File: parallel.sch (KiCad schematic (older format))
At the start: 74 parts, among them CN300 KEYBOARD, CN301 DB25F, CN302 DB23F, CN303 Conn_02x17_Odd_Even, J300 Conn_01x03_Male, J301 DF1:, Q301 2N3904, U102 GARY5719, U108 74LS74A, U203 74LS38, U300 CIA8520, U302 74LS32, U303 74F08, U607 74LS08, U900 74F00

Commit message: Update footprints
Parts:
- C203, C259, C260, C261, C300, C302, C303, C322, C323, C607, C909, C916: footprint (none) -> Capacitor_THT:C_Rect_L11.0mm_W2.8mm_P10.00mm_MKT
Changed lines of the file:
@@
 F 0 "C261" H 9115 1846 50  0000 L CNN
 F 1 "100pF" H 9115 1755 50  0000 L CNN
-F 2 "" H 9038 1650 50  0001 C CNN
+F 2 "Capacitor_THT:C_Rect_L11.0mm_W2.8mm_P10.00mm_MKT" H 9038 1650 50  0001 C CNN
 F 3 "~" H 9000 1800 50  0001 C CNN
 	1    9000 1800
@@
 F 0 "C260" H 9565 1846 50  0000 L CNN
 F 1 "100pF" H 9565 1755 50  0000 L CNN
-F 2 "" H 9488 1650 50  0001 C CNN
+F 2 "Capacitor_THT:C_Rect_L11.0mm_W2.8mm_P10.00mm_MKT" H 9488 1650 50  0001 C CNN
 F 3 "~" H 9450 1800 50  0001 C CNN
 	1    9450 1800
@@
 F 0 "C259" H 10015 1846 50  0000 L CNN
 F 1 "100pF" H 10015 1755 50  0000 L CNN
-F 2 "" H 9938 1650 50  0001 C CNN
+F 2 "Capacitor_THT:C_Rect_L11.0mm_W2.8mm_P10.00mm_MKT" H 9938 1650 50  0001 C CNN
 F 3 "~" H 9900 1800 50  0001 C CNN
 	1    9900 1800
@@
 F 0 "C909" H 3415 6046 50  0000 L CNN
 F 1 "0.1uF" H 3415 5955 50  0000 L CNN
-F 2 "" H 3338 5850 50  0001 C CNN
+F 2 "Capacitor_THT:C_Rect_L11.0mm_W2.8mm_P10.00mm_MKT" H 3338 5850 50  0001 C CNN
 F 3 "~" H 3300 6000 50  0001 C CNN
 	1    3300 6000
@@
 F 0 "C916" H 8215 7446 50  0000 L CNN
 F 1 "0.1uF" H 8215 7355 50  0000 L CNN
-F 2 "" H 8138 7250 50  0001 C CNN
+F 2 "Capacitor_THT:C_Rect_L11.0mm_W2.8mm_P10.00mm_MKT" H 8138 7250 50  0001 C CNN
 F 3 "~" H 8100 7400 50  0001 C CNN
 	1    8100 7400
@@
 F 0 "C322" H 15265 2046 50  0000 L CNN
 F 1 "0.01uF" H 15265 1955 50  0000 L CNN
-F 2 "" H 15188 1850 50  0001 C CNN
+F 2 "Capacitor_THT:C_Rect_L11.0mm_W2.8mm_P10.00mm_MKT" H 15188 1850 50  0001 C CNN
 F 3 "~" H 15150 2000 50  0001 C CNN
 	1    15150 2000
@@
 F 0 "C323" H 15765 2046 50  0000 L CNN
 F 1 "0.01uF" H 15765 1955 50  0000 L CNN
-F 2 "" H 15688 1850 50  0001 C CNN
+F 2 "Capacitor_THT:C_Rect_L11.0mm_W2.8mm_P10.00mm_MKT" H 15688 1850 50  0001 C CNN
 F 3 "~" H 15650 2000 50  0001 C CNN
 	1    15650 2000
@@
 F 0 "C300" H 2865 2846 50  0000 L CNN
 F 1 "0.1uF" H 2865 2755 50  0000 L CNN
-F 2 "" H 2788 2650 50  0001 C CNN
+F 2 "Capacitor_THT:C_Rect_L11.0mm_W2.8mm_P10.00mm_MKT" H 2788 2650 50  0001 C CNN
 F 3 "~" H 2750 2800 50  0001 C CNN
 	1    2750 2800
@@
 F 0 "C203" H 2815 10046 50  0000 L CNN
 F 1 "0.1uF" H 2815 9955 50  0000 L CNN
-F 2 "" H 2738 9850 50  0001 C CNN
+F 2 "Capacitor_THT:C_Rect_L11.0mm_W2.8mm_P10.00mm_MKT" H 2738 9850 50  0001 C CNN
 F 3 "~" H 2700 10000 50  0001 C CNN
 	1    2700 10000
@@
 F 0 "C302" H 4515 10046 50  0000 L CNN
 F 1 "0.1uF" H 4515 9955 50  0000 L CNN
-F 2 "" H 4438 9850 50  0001 C CNN
+F 2 "Capacitor_THT:C_Rect_L11.0mm_W2.8mm_P10.00mm_MKT" H 4438 9850 50  0001 C CNN
 F 3 "~" H 4400 10000 50  0001 C CNN
 	1    4400 10000
@@
 F 0 "C303" H 6215 10046 50  0000 L CNN
 F 1 "0.1uF" H 6215 9955 50  0000 L CNN
-F 2 "" H 6138 9850 50  0001 C CNN
+F 2 "Capacitor_THT:C_Rect_L11.0mm_W2.8mm_P10.00mm_MKT" H 6138 9850 50  0001 C CNN
 F 3 "~" H 6100 10000 50  0001 C CNN
 	1    6100 10000
@@
 F 0 "C607" H 7715 9996 50  0000 L CNN
 F 1 "0.1uF" H 7715 9905 50  0000 L CNN
-F 2 "" H 7638 9800 50  0001 C CNN
+F 2 "Capacitor_THT:C_Rect_L11.0mm_W2.8mm_P10.00mm_MKT" H 7638 9800 50  0001 C CNN
 F 3 "~" H 7600 9950 50  0001 C CNN
 	1    7600 9950
@@
 Wire Wire Line
 	15200 3600 15200 3650
+Text Notes 9650 5400 1    197  ~ 0
+PARALLEL
+Text Notes 13600 1950 2    197  ~ 0
+EXT FLOPPY
 Wire Bus Line
 	1200 4450 3050 4450
@@
 Wire Bus Line
 	4950 5000 4950 5900
-Text Notes 9650 5400 1    197  ~ 0
-PARALLEL
-Text Notes 13600 1950 2    197  ~ 0
-EXT FLOPPY
 $EndSCHEMATC

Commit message: Components associations finished; regenered netlist and pdf
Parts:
- CN300: footprint (none) -> d_amiga:DIN_5_KBD
- CN302: footprint (none) -> d_amiga:DSUB-23_Male_Horizontal_P2.77x2.84mm_EdgePinOffset7.70mm_Housed_MountingHolesOffset9.12mm
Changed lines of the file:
@@
 F 0 "CN302" V 12785 2450 50  0000 C CNN
 F 1 "DB23F" V 12876 2450 50  0000 C CNN
-F 2 "" H 13100 2350 50  0001 C CNN
+F 2 "d_amiga:DSUB-23_Male_Horizontal_P2.77x2.84mm_EdgePinOffset7.70mm_Housed_MountingHolesOffset9.12mm" H 13100 2350 50  0001 C CNN
 F 3 " ~" H 13100 2350 50  0001 C CNN
 F 4 "Female" V 13150 2450 50  0001 C CNN "Gender"
@@
 F 0 "CN300" H 10100 833 50  0000 C CNN
 F 1 "KEYBOARD" H 10100 924 50  0000 C CNN
-F 2 "" H 10100 1200 50  0001 C CNN
+F 2 "d_amiga:DIN_5_KBD" H 10100 1200 50  0001 C CNN
 F 3 "http://www.mouser.com/ds/2/18/40_c091_abd_e-75918.pdf" H 10100 1200 50  0001 C CNN
 F 4 "Female" H 10100 1200 50  0001 C CNN "Gender"

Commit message: More placement
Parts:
- CN303: footprint Connector_PinSocket_2.54mm:PinSocket_2x17_P2.54mm_Vertical -> Connector_PinHeader_2.54mm:PinHeader_2x17_P2.54mm_Vertical
- J300: footprint Connector_PinSocket_2.54mm:PinSocket_1x03_P2.54mm_Vertical -> Connector_PinHeader_2.54mm:PinHeader_1x03_P2.54mm_Vertical
- J301: footprint Connector_PinSocket_2.54mm:PinSocket_2x01_P2.54mm_Vertical -> Connector_PinHeader_2.54mm:PinHeader_2x01_P2.54mm_Vertical
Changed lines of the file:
@@
 F 0 "CN303" H 15700 6325 50  0000 C CNN
 F 1 "Conn_02x17_Odd_Even" H 15700 6326 50  0001 C CNN
-F 2 "Connector_PinSocket_2.54mm:PinSocket_2x17_P2.54mm_Vertical" H 15650 5400 50  0001 C CNN
+F 2 "Connector_PinHeader_2.54mm:PinHeader_2x17_P2.54mm_Vertical" H 15650 5400 50  0001 C CNN
 F 3 "~" H 15650 5400 50  0001 C CNN
 F 4 "Male" H 15650 5400 50  0001 C CNN "Gender"
@@
 F 0 "J300" V 2058 5812 50  0000 R CNN
 F 1 "Conn_01x03_Male" V 2013 5812 50  0001 R CNN
-F 2 "Connector_PinSocket_2.54mm:PinSocket_1x03_P2.54mm_Vertical" H 1950 6000 50  0001 C CNN
+F 2 "Connector_PinHeader_2.54mm:PinHeader_1x03_P2.54mm_Vertical" H 1950 6000 50  0001 C CNN
 F 3 "~" H 1950 6000 50  0001 C CNN
 	1    1950 6000
@@
 F 0 "J301" H 15572 6882 50  0000 R CNN
 F 1 "DF1:" H 15572 6973 50  0000 R CNN
-F 2 "Connector_PinSocket_2.54mm:PinSocket_2x01_P2.54mm_Vertical" H 15600 7000 50  0001 C CNN
+F 2 "Connector_PinHeader_2.54mm:PinHeader_2x01_P2.54mm_Vertical" H 15600 7000 50  0001 C CNN
 F 3 "~" H 15600 7000 50  0001 C CNN
 	1    15600 7000

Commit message: first placement pass is done
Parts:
- C912: footprint Capacitor_THT:CP_Radial_D10.0mm_P5.00mm -> Capacitor_THT:CP_Radial_D8.0mm_P5.00mm
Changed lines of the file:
@@
 F 0 "C912" H 10468 1846 50  0000 L CNN
 F 1 "470uF 25v" H 10468 1755 50  0000 L CNN
-F 2 "Capacitor_THT:CP_Radial_D10.0mm_P5.00mm" H 10388 1650 50  0001 C CNN
+F 2 "Capacitor_THT:CP_Radial_D8.0mm_P5.00mm" H 10388 1650 50  0001 C CNN
 F 3 "~" H 10350 1800 50  0001 C CNN
 	1    10350 1800

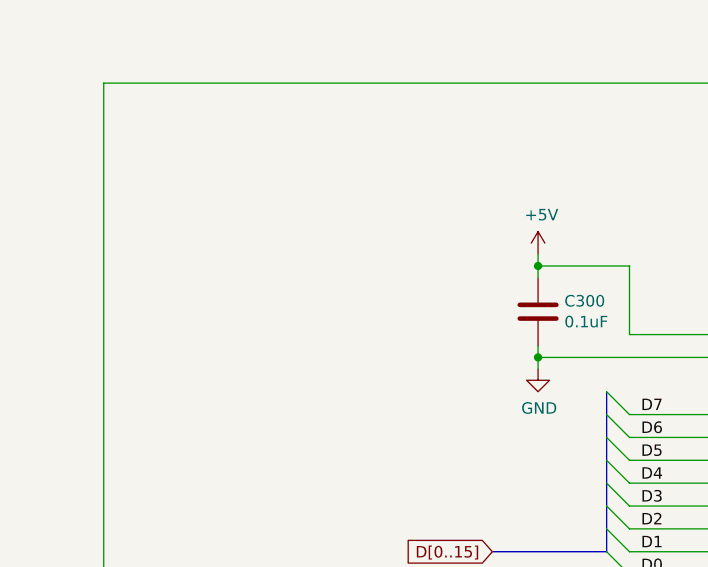
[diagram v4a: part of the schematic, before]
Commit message: mod: breakout INT2/OVR to pin header
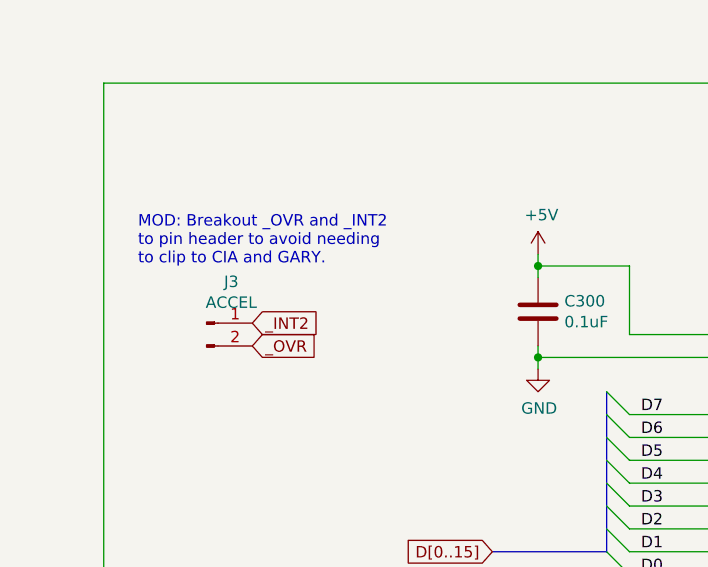
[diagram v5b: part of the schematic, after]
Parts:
- added J3: ACCEL, Connector_PinHeader_2.54mm:PinHeader_1x02_P2.54mm_Vertical, symbol Connector:Conn_01x02_Male
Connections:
- net _INT2: now also J3.1 (Pin_1)
- new net _OVR: J3.2 (Pin_2)
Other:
- note added: "MOD: Breakout _OVR and _INT2 \nto pin header to avoid needing \nto clip to CIA and GARY."
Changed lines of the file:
@@
 Text Notes 13600 1950 2    197  ~ 0
 EXT FLOPPY
+$Comp
+L Connector:Conn_01x02_Male J3
+U 1 1 5E049EEE
+P 1300 2850
+F 0 "J3" H 1408 3031 50  0000 C CNN
+F 1 "ACCEL" H 1408 2940 50  0000 C CNN
+F 2 "Connector_PinHeader_2.54mm:PinHeader_1x02_P2.54mm_Vertical" H 1300 2850 50  0001 C CNN
+F 3 "~" H 1300 2850 50  0001 C CNN
+	1    1300 2850
+	1    0    0    -1
+$EndComp
+Text GLabel 1500 2850 2    50   Input ~ 0
+_INT2
+Text GLabel 1500 2950 2    50   Input ~ 0
+_OVR
+Text Notes 1000 2600 0    50   ~ 0
+MOD: Breakout _OVR and _INT2 \nto pin header to avoid needing \nto clip to CIA and GARY.
 Wire Bus Line
 	1200 4450 3050 4450

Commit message: Make caps footprint smaller
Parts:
- C203, C259, C260, C261, C300, C302, C303, C322, C323, C607, C909, C916: footprint Capacitor_THT:C_Rect_L11.0mm_W2.8mm_P10.00mm_MKT -> Capacitor_THT:C_Rect_L11.5mm_W2.0mm_P10.00mm_MKT
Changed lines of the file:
@@
 F 0 "C261" H 9115 1846 50  0000 L CNN
 F 1 "100pF" H 9115 1755 50  0000 L CNN
-F 2 "Capacitor_THT:C_Rect_L11.0mm_W2.8mm_P10.00mm_MKT" H 9038 1650 50  0001 C CNN
+F 2 "Capacitor_THT:C_Rect_L11.5mm_W2.0mm_P10.00mm_MKT" H 9038 1650 50  0001 C CNN
 F 3 "~" H 9000 1800 50  0001 C CNN
 	1    9000 1800
@@
 F 0 "C260" H 9565 1846 50  0000 L CNN
 F 1 "100pF" H 9565 1755 50  0000 L CNN
-F 2 "Capacitor_THT:C_Rect_L11.0mm_W2.8mm_P10.00mm_MKT" H 9488 1650 50  0001 C CNN
+F 2 "Capacitor_THT:C_Rect_L11.5mm_W2.0mm_P10.00mm_MKT" H 9488 1650 50  0001 C CNN
 F 3 "~" H 9450 1800 50  0001 C CNN
 	1    9450 1800
@@
 F 0 "C259" H 10015 1846 50  0000 L CNN
 F 1 "100pF" H 10015 1755 50  0000 L CNN
-F 2 "Capacitor_THT:C_Rect_L11.0mm_W2.8mm_P10.00mm_MKT" H 9938 1650 50  0001 C CNN
+F 2 "Capacitor_THT:C_Rect_L11.5mm_W2.0mm_P10.00mm_MKT" H 9938 1650 50  0001 C CNN
 F 3 "~" H 9900 1800 50  0001 C CNN
 	1    9900 1800
@@
 F 0 "C909" H 3415 6046 50  0000 L CNN
 F 1 "0.1uF" H 3415 5955 50  0000 L CNN
-F 2 "Capacitor_THT:C_Rect_L11.0mm_W2.8mm_P10.00mm_MKT" H 3338 5850 50  0001 C CNN
+F 2 "Capacitor_THT:C_Rect_L11.5mm_W2.0mm_P10.00mm_MKT" H 3338 5850 50  0001 C CNN
 F 3 "~" H 3300 6000 50  0001 C CNN
 	1    3300 6000
@@
 F 0 "C916" H 8215 7446 50  0000 L CNN
 F 1 "0.1uF" H 8215 7355 50  0000 L CNN
-F 2 "Capacitor_THT:C_Rect_L11.0mm_W2.8mm_P10.00mm_MKT" H 8138 7250 50  0001 C CNN
+F 2 "Capacitor_THT:C_Rect_L11.5mm_W2.0mm_P10.00mm_MKT" H 8138 7250 50  0001 C CNN
 F 3 "~" H 8100 7400 50  0001 C CNN
 	1    8100 7400
@@
 F 0 "C322" H 15265 2046 50  0000 L CNN
 F 1 "0.01uF" H 15265 1955 50  0000 L CNN
-F 2 "Capacitor_THT:C_Rect_L11.0mm_W2.8mm_P10.00mm_MKT" H 15188 1850 50  0001 C CNN
+F 2 "Capacitor_THT:C_Rect_L11.5mm_W2.0mm_P10.00mm_MKT" H 15188 1850 50  0001 C CNN
 F 3 "~" H 15150 2000 50  0001 C CNN
 	1    15150 2000
@@
 F 0 "C323" H 15765 2046 50  0000 L CNN
 F 1 "0.01uF" H 15765 1955 50  0000 L CNN
-F 2 "Capacitor_THT:C_Rect_L11.0mm_W2.8mm_P10.00mm_MKT" H 15688 1850 50  0001 C CNN
+F 2 "Capacitor_THT:C_Rect_L11.5mm_W2.0mm_P10.00mm_MKT" H 15688 1850 50  0001 C CNN
 F 3 "~" H 15650 2000 50  0001 C CNN
 	1    15650 2000
@@
 F 0 "C300" H 2865 2846 50  0000 L CNN
 F 1 "0.1uF" H 2865 2755 50  0000 L CNN
-F 2 "Capacitor_THT:C_Rect_L11.0mm_W2.8mm_P10.00mm_MKT" H 2788 2650 50  0001 C CNN
+F 2 "Capacitor_THT:C_Rect_L11.5mm_W2.0mm_P10.00mm_MKT" H 2788 2650 50  0001 C CNN
 F 3 "~" H 2750 2800 50  0001 C CNN
 	1    2750 2800
@@
 F 0 "C203" H 2815 10046 50  0000 L CNN
 F 1 "0.1uF" H 2815 9955 50  0000 L CNN
-F 2 "Capacitor_THT:C_Rect_L11.0mm_W2.8mm_P10.00mm_MKT" H 2738 9850 50  0001 C CNN
+F 2 "Capacitor_THT:C_Rect_L11.5mm_W2.0mm_P10.00mm_MKT" H 2738 9850 50  0001 C CNN
 F 3 "~" H 2700 10000 50  0001 C CNN
 	1    2700 10000
@@
 F 0 "C302" H 4515 10046 50  0000 L CNN
 F 1 "0.1uF" H 4515 9955 50  0000 L CNN
-F 2 "Capacitor_THT:C_Rect_L11.0mm_W2.8mm_P10.00mm_MKT" H 4438 9850 50  0001 C CNN
+F 2 "Capacitor_THT:C_Rect_L11.5mm_W2.0mm_P10.00mm_MKT" H 4438 9850 50  0001 C CNN
 F 3 "~" H 4400 10000 50  0001 C CNN
 	1    4400 10000
@@
 F 0 "C303" H 6215 10046 50  0000 L CNN
 F 1 "0.1uF" H 6215 9955 50  0000 L CNN
-F 2 "Capacitor_THT:C_Rect_L11.0mm_W2.8mm_P10.00mm_MKT" H 6138 9850 50  0001 C CNN
+F 2 "Capacitor_THT:C_Rect_L11.5mm_W2.0mm_P10.00mm_MKT" H 6138 9850 50  0001 C CNN
 F 3 "~" H 6100 10000 50  0001 C CNN
 	1    6100 10000
@@
 F 0 "C607" H 7715 9996 50  0000 L CNN
 F 1 "0.1uF" H 7715 9905 50  0000 L CNN
-F 2 "Capacitor_THT:C_Rect_L11.0mm_W2.8mm_P10.00mm_MKT" H 7638 9800 50  0001 C CNN
+F 2 "Capacitor_THT:C_Rect_L11.5mm_W2.0mm_P10.00mm_MKT" H 7638 9800 50  0001 C CNN
 F 3 "~" H 7600 9950 50  0001 C CNN
 	1    7600 9950

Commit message: All components have been realigned; plus small sizes changes
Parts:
- F3, F4: footprint Fuse:Fuse_Littelfuse-LVR100 -> Capacitor_THT:C_Rect_L11.5mm_W2.0mm_P10.00mm_MKT
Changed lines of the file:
@@
 F 0 "F3" V 14445 1650 50  0000 C CNN
 F 1 "Fuse" V 14444 1650 50  0001 C CNN
-F 2 "Fuse:Fuse_Littelfuse-LVR100" V 14480 1650 50  0001 C CNN
+F 2 "Capacitor_THT:C_Rect_L11.5mm_W2.0mm_P10.00mm_MKT" V 14480 1650 50  0001 C CNN
 F 3 "~" H 14550 1650 50  0001 C CNN
 	1    14550 1650
@@
 F 0 "F4" V 14445 1450 50  0000 C CNN
 F 1 "Fuse" V 14444 1450 50  0001 C CNN
-F 2 "Fuse:Fuse_Littelfuse-LVR100" V 14480 1450 50  0001 C CNN
+F 2 "Capacitor_THT:C_Rect_L11.5mm_W2.0mm_P10.00mm_MKT" V 14480 1450 50  0001 C CNN
 F 3 "~" H 14550 1450 50  0001 C CNN
 	1    14550 1450
